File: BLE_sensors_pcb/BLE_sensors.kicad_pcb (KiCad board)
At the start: 2 copper layers, 2 parts, among them U1 BME280, U2 LSM303AHTR

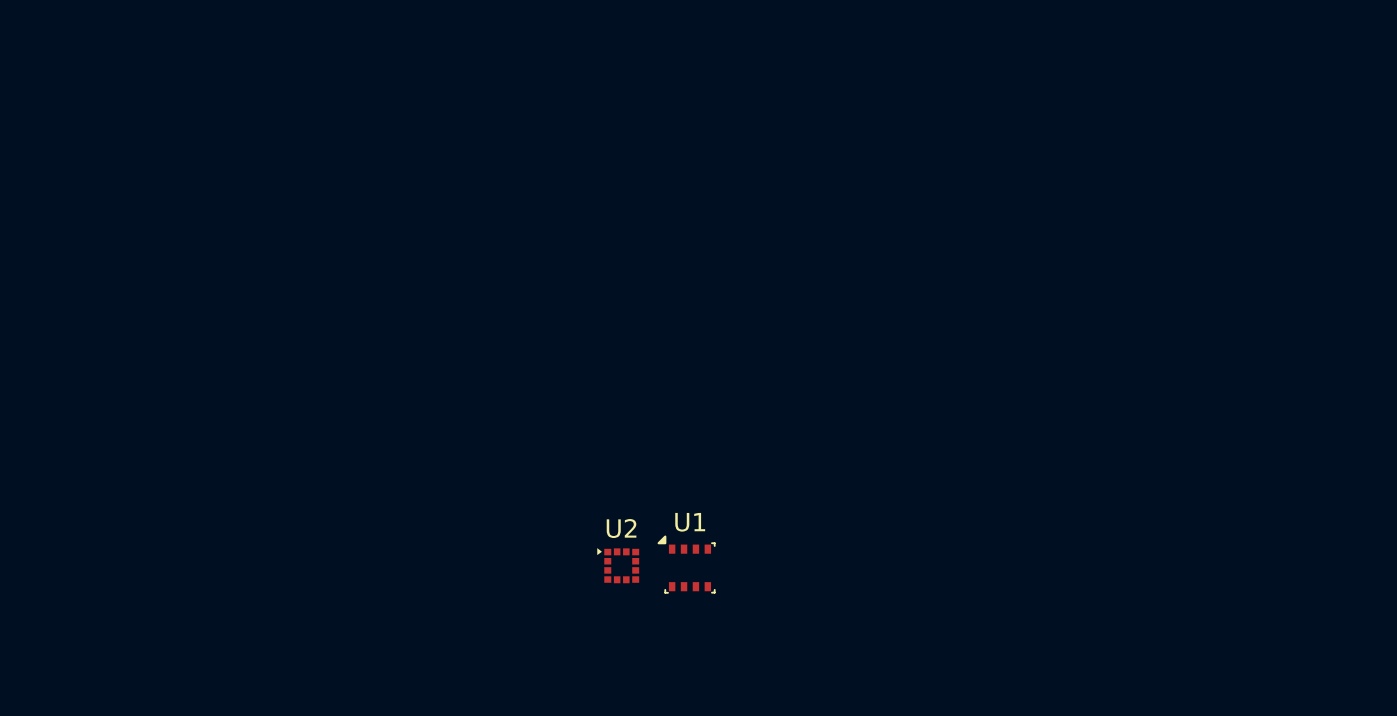
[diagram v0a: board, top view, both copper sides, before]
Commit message: added BM15C
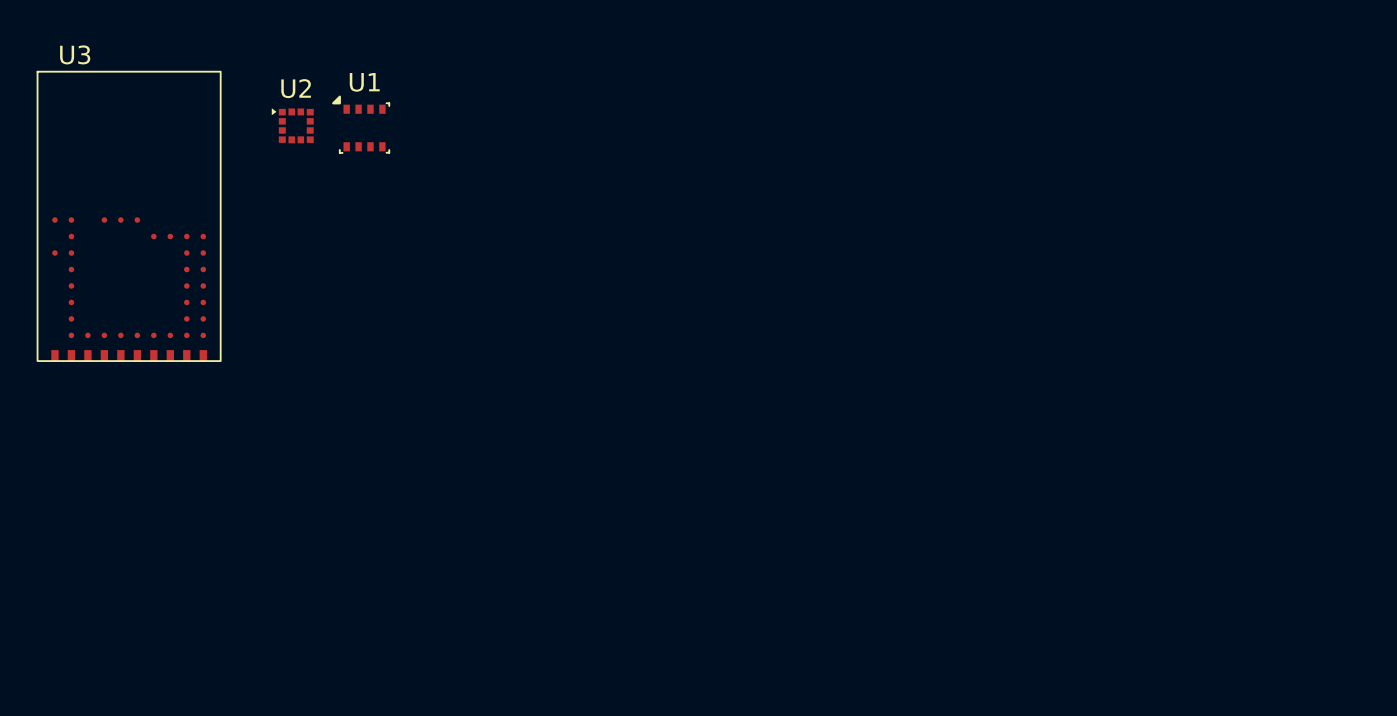
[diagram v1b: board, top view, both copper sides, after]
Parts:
- added U3: ~, My_Libraries:BM15C, F.Cu at (34.6, 41.1)
- moved U2 29.9 mm to (38.7, 28.2)
- moved U1 29.9 mm to (42.5, 28.3)

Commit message: added datashet for me54bs01 and dev board and the me54bs01 to the kicad project
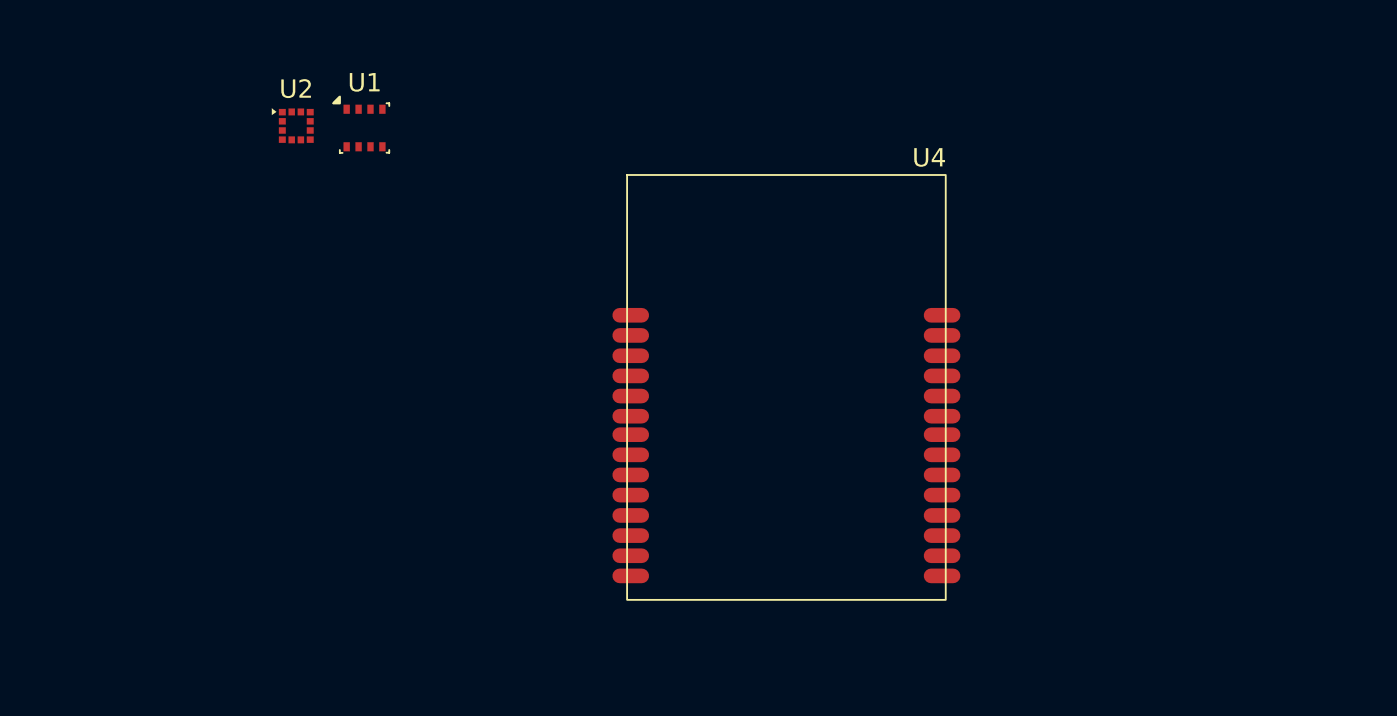
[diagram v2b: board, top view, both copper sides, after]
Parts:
- removed U3: ~, My_Libraries:BM15C
- added U4: ~, My_Libraries:Untitled, F.Cu at (65.5, 42.5)

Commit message: Refactor schematic and added power supplpy
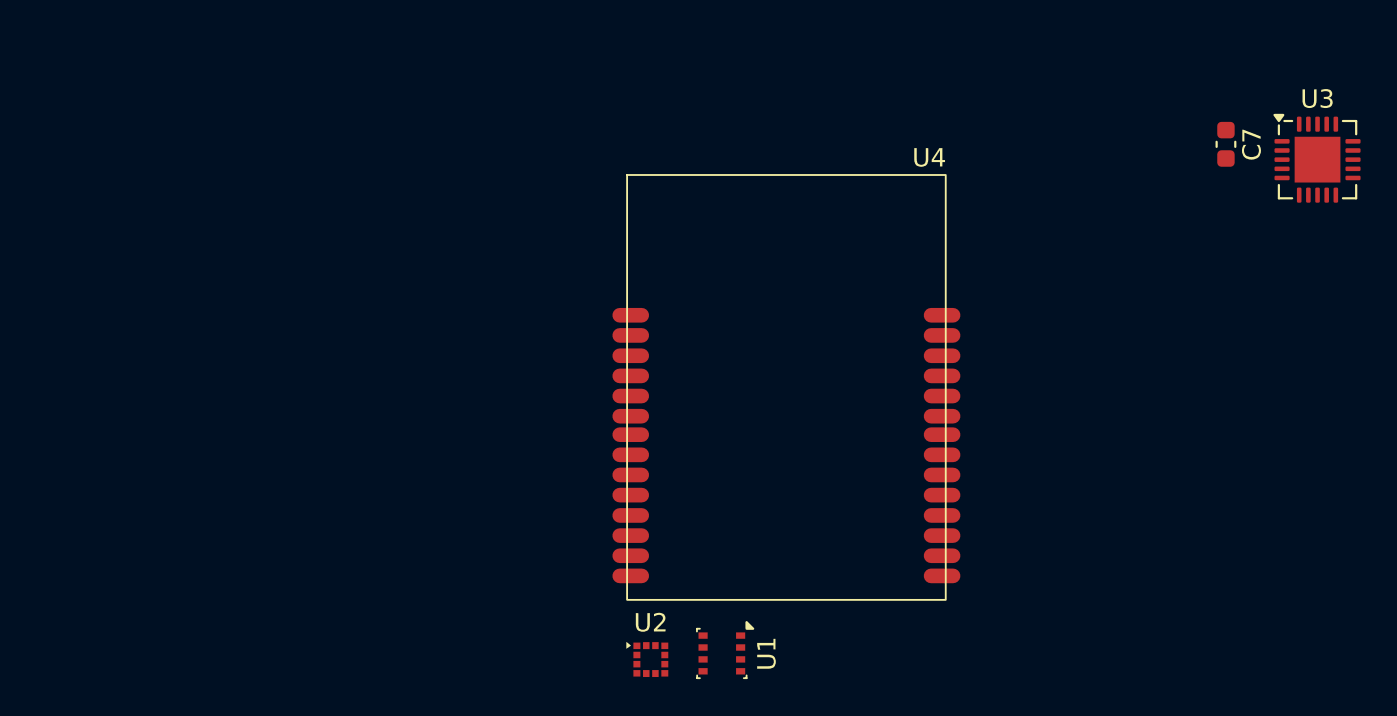
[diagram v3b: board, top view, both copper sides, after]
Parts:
- added C7: C_Small, Capacitor_SMD:C_0603_1608Metric, F.Cu at (89.5, 29.2)
- added U3: MCP73871, Package_DFN_QFN:QFN-20-1EP_4x4mm_P0.5mm_EP2.5x2.5mm, F.Cu at (94.5, 30.1)
- U4: footprint My_Libraries:Untitled -> My_Libraries:ME54BS01
- moved U2 35.0 mm to (58.1, 57.4)
- moved U1 34.7 mm to (62.0, 57.0), turned to -90 degrees
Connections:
- U1 pad 1: unconnected-(U1-GND-Pad1) -> GND
- U1 pad 2: unconnected-(U1-CSB-Pad2) -> Net-(U1-CSB)
- U1 pad 3: unconnected-(U1-SDI-Pad3) -> /SDA
- U1 pad 4: unconnected-(U1-SCK-Pad4) -> /SCL
- U1 pad 5: unconnected-(U1-SDO-Pad5) -> GND
- U1 pad 6: unconnected-(U1-VDDIO-Pad6) -> Net-(U1-CSB)
- U1 pad 7: unconnected-(U1-GND-Pad7) -> GND
- U1 pad 8: unconnected-(U1-VDD-Pad8) -> Net-(U1-VDD)
- U2 pad 1: unconnected-(U2-SCL/SPC-Pad1) -> /SPC
- U2 pad 10: unconnected-(U2-Vdd_IO-Pad10) -> /Vdd_IO
- U2 pad 11: unconnected-(U2-INT2_XL-Pad11) -> /INT2_XL
- U2 pad 12: unconnected-(U2-INT1_XL-Pad12) -> /INT1_XL
- U2 pad 2: unconnected-(U2-CS-Pad2) -> /CS
- U2 pad 3: unconnected-(U2-RESERVED-Pad3) -> GND
- U2 pad 4: unconnected-(U2-SDA/SDI/SDO-Pad4) -> /SDI
- U2 pad 5: unconnected-(U2-C1-Pad5) -> Net-(U2-C1)
- U2 pad 6: unconnected-(U2-GND-Pad6) -> GND
- U2 pad 7: unconnected-(U2-INT_MAG/DRDY-Pad7) -> /INT_MAG/DRDY
- U2 pad 8: unconnected-(U2-GND-Pad8) -> GND
- U2 pad 9: unconnected-(U2-Vdd-Pad9) -> /Vdd
- U4 pad 1: unconnected-(U4-GND-Pad1) -> GND
- U4 pad 13: unconnected-(U4-GND-Pad13) -> GND
- U4 pad 18: unconnected-(U4-P2.06-Pad18) -> /INT_MAG/DRDY
- U4 pad 19: unconnected-(U4-P2.07-Pad19) -> /INT2_XL
- U4 pad 21: unconnected-(U4-P2.09-Pad21) -> /INT1_XL
- U4 pad 22: unconnected-(U4-P2.10-Pad22) -> /SDI
- U4 pad 23: unconnected-(U4-P0.00-Pad23) -> /SPC
- U4 pad 24: unconnected-(U4-P0.01-Pad24) -> /CS
- U4 pad 27: unconnected-(U4-P0.02-Pad27) -> /SCL
- U4 pad 28: unconnected-(U4-P0.03-Pad28) -> /SDA
